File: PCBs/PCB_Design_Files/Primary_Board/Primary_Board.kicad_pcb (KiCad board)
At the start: 4 copper layers, 40.3 x 57.1 mm, 106 parts, among them J1 Conn_FFC_8pin, J2 Conn_01x08_Pin, U1 OPA381, U11 TMUX1104DGSR, U12 TMUX1133PWR, U13 TMUX1133PWR, U14 TMUX1133PWR, U15 TMUX1133PWR, U2 TLV9002, U3 TLV9002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

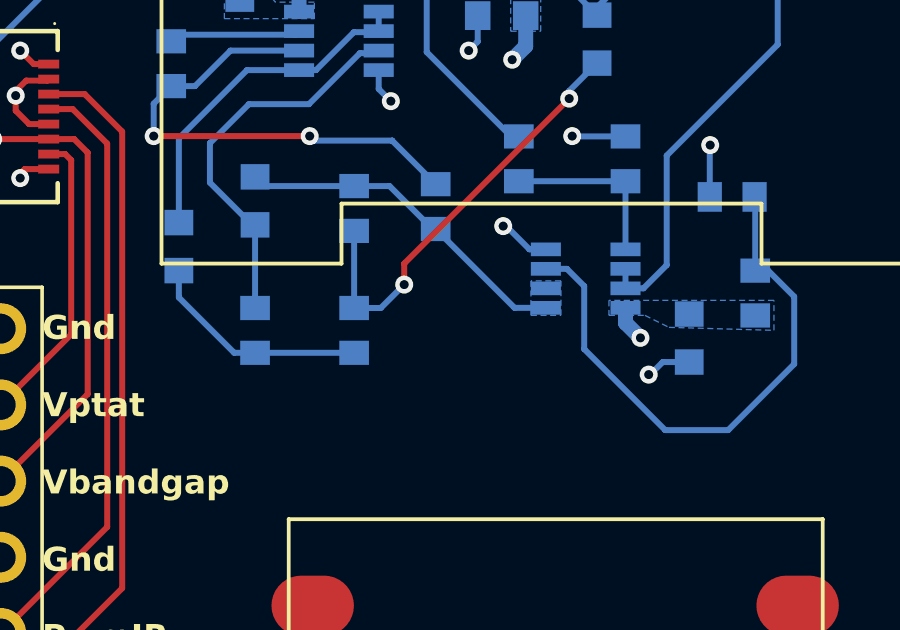
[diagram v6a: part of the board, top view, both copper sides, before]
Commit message: added 3rd order filter
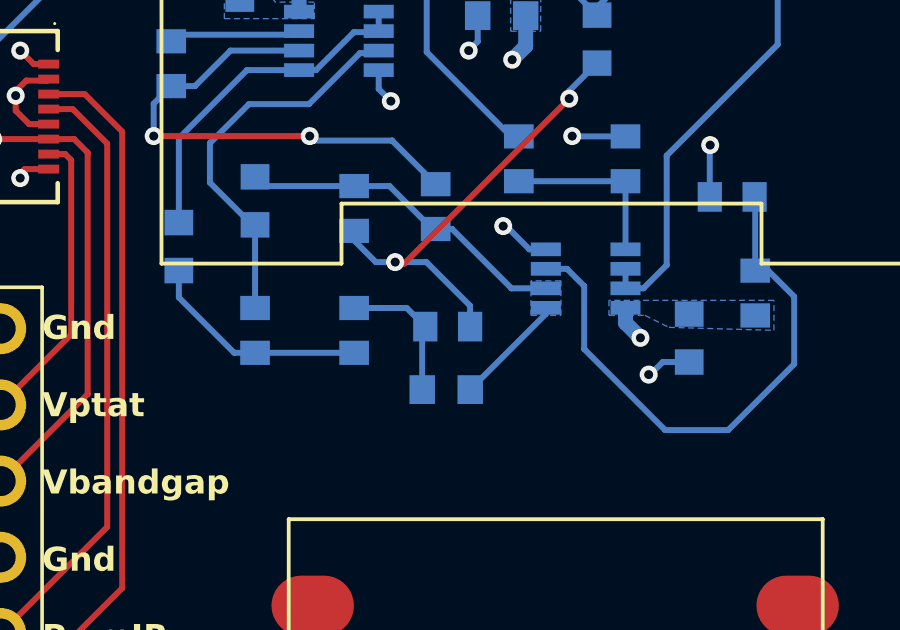
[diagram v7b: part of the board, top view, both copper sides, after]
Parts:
- added C68: 220n, Project Footprints:0603_capacitor, B.Cu at (143.0, 104.7)
- added R17: 100k, Project Footprints:0603_resistor, B.Cu at (143.1, 102.5)
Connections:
- R4 pad 1: Net-(C5-Pad2) -> Net-(C68-Pad1)
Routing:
- net Net-(C68-Pad1): track 0.00 -> 4.77 mm
- net /AFE/+1.65V: track 12.0 -> 15.5 mm
- net Net-(C5-Pad2): track 14.6 -> 15.4 mm

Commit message: updated AFE pcb
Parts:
- removed C4: .1u, Project Footprints:0603_capacitor
- removed U3: TLV9002, Project Footprints:TLV9002
- added JP1: ADC_BYPASS, Jumper:SolderJumper-2_P1.3mm_Open_Pad1.0x1.5mm, F.Cu at (111.5, 118.0)
- R10: value 35k -> 40k
- R4, R5: value 120k -> 100k
- moved C68 2.38 mm to (141.4, 102.8), turned to -90 degrees
- moved R17 0.91 mm to (143.9, 102.7), turned to -90 degrees
- moved R4 0.88 mm to (139.1, 102.7)
- moved R5 0.23 mm to (136.4, 102.7)
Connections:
- C2 pad 2: /AFE/TIA_Out -> /AFE/TIA_OUT
- C5 pad 1: /AFE/TIA_Out -> /AFE/TIA_OUT
- J1 pad 6: /V_bandgap -> /V_ptat
- J1 pad 7: /V_ptat -> /V_bandgap
- J2 pad 6: /V_bandgap -> /V_ptat
- J2 pad 7: /V_ptat -> /V_bandgap
- R13 pad 1: /ADC/ADC_Input2 -> /AFE/TIA_OUT
- R2 pad 2: /AFE/TIA_Out -> /AFE/TIA_OUT
- U1 pad 6: /AFE/TIA_Out -> /AFE/TIA_OUT
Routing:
- net /AFE/TIA_Out: track 17.2 -> 0.00 mm
- net /AFE/TIA_OUT: track 0.00 -> 16.0 mm
- net GND: track 24.2 -> 20.1 mm, vias 15 -> 12
- net /V_ptat: track 9.87 -> 13.6 mm
- net /AFE/+1.65V: track 15.5 -> 19.1 mm
- net /V_bandgap: track 42.1 -> 38.6 mm
- net +3V3: track 6.70 -> 5.20 mm, vias 5 -> 4
- net Net-(C68-Pad1): track 4.77 -> 5.55 mm
- net /ADC/ADC_Input2: track 0.65 -> 0.00 mm
- net Net-(U3-IN2-): track 0.65 -> 0.00 mm
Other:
- board text added: "Gnd Vbandgap Vptat Gnd PwmIR PwmRed Gnd 3v3"
- board text removed: "Gnd Vptat Vbandgap Gnd PwmIR PwmRed Gnd 3v3"
